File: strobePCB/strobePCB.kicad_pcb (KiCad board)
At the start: 2 copper layers, 18.8 x 28.8 mm, 14 parts, among them J1 Conn_01x02_Socket

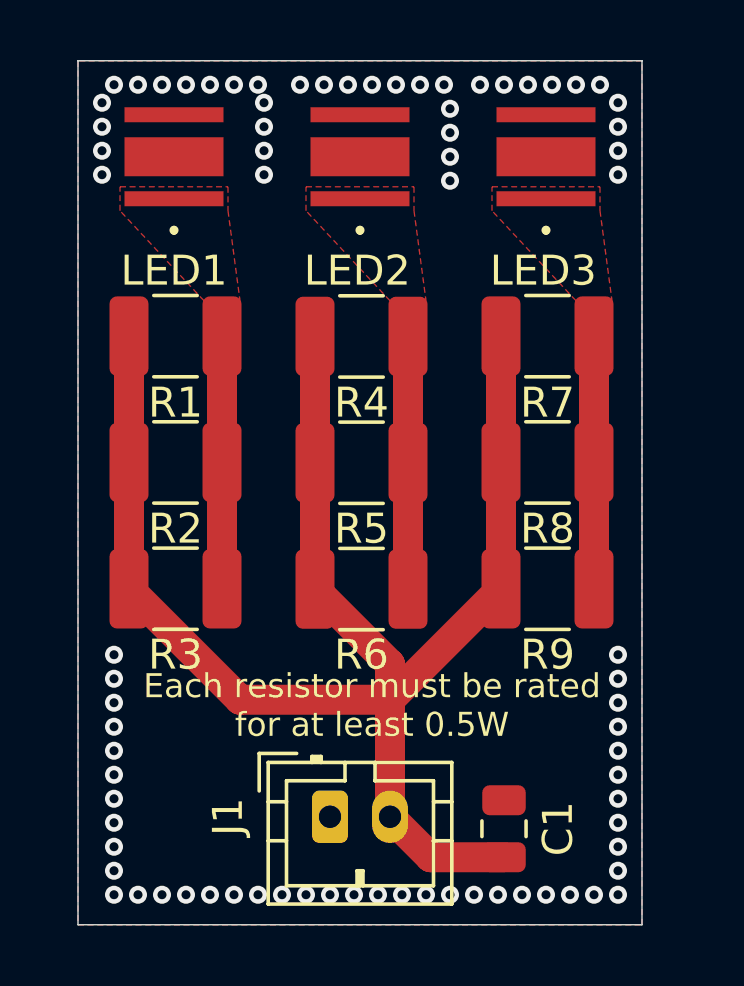
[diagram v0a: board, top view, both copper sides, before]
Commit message: Routed RP2350B w/ dependencies + power circuit
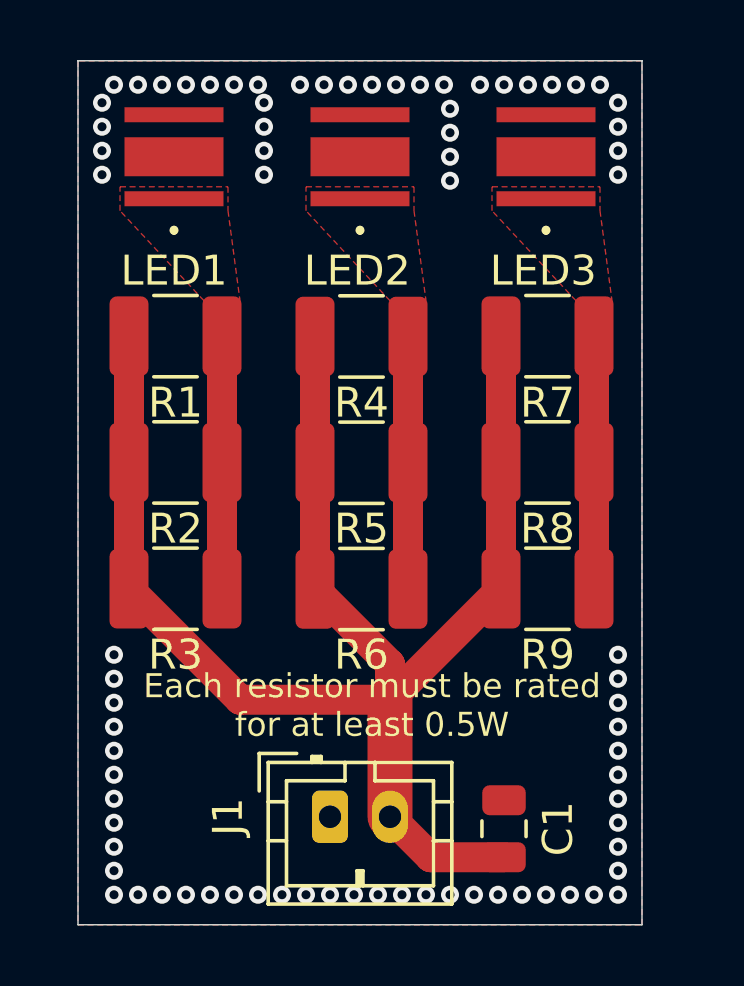
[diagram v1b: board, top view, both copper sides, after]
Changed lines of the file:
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@@
 		(start 110 77.4)
 		(end 110 73.5)
-		(width 1)
+		(width 1.5)
 		(layer "F.Cu")
 		(net 1)
